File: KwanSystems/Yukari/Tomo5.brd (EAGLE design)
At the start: 43 parts, among them J101 USB_MICROB_JST, U101 FT232RLSSOP, U401 ATMEGA328P, U501 FGPMMOPA6H, U601 MPU9250, X501 uFL, Y401 16MHz

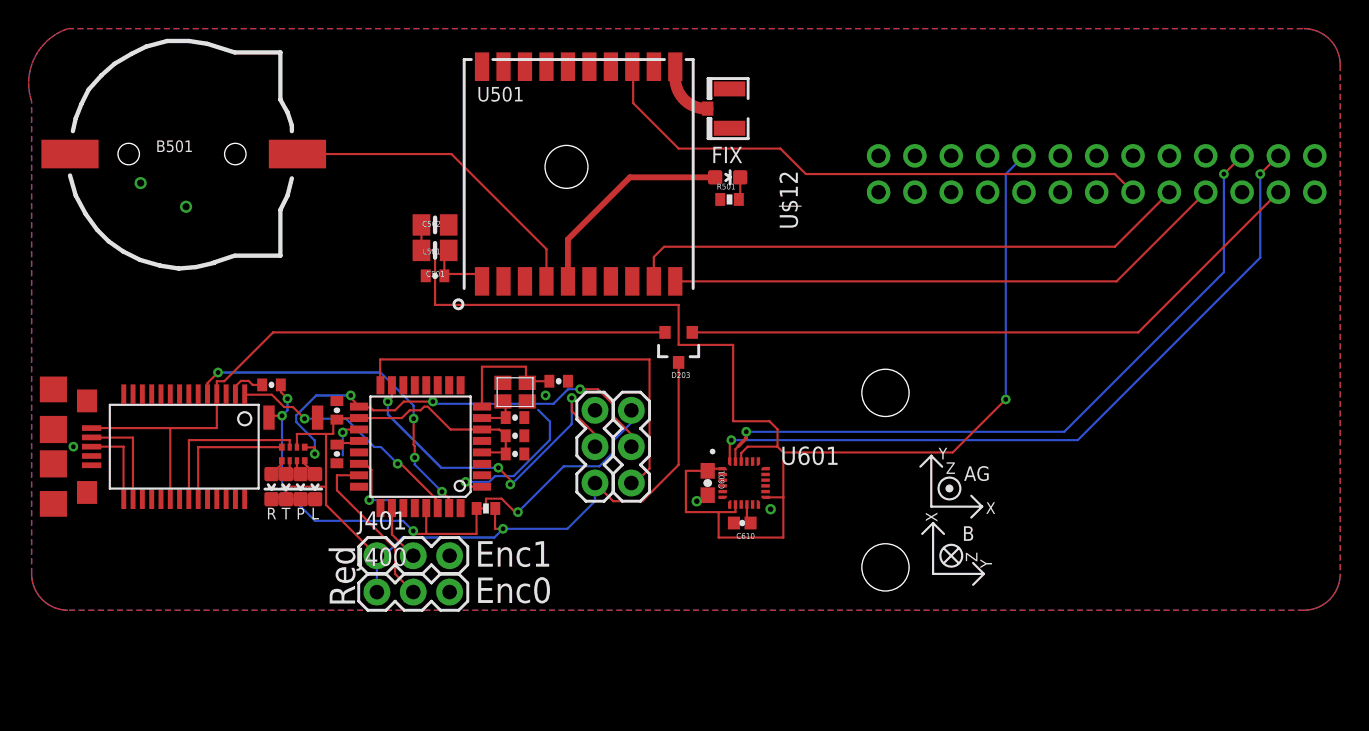
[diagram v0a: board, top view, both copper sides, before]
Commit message: Added Adafruit stuff
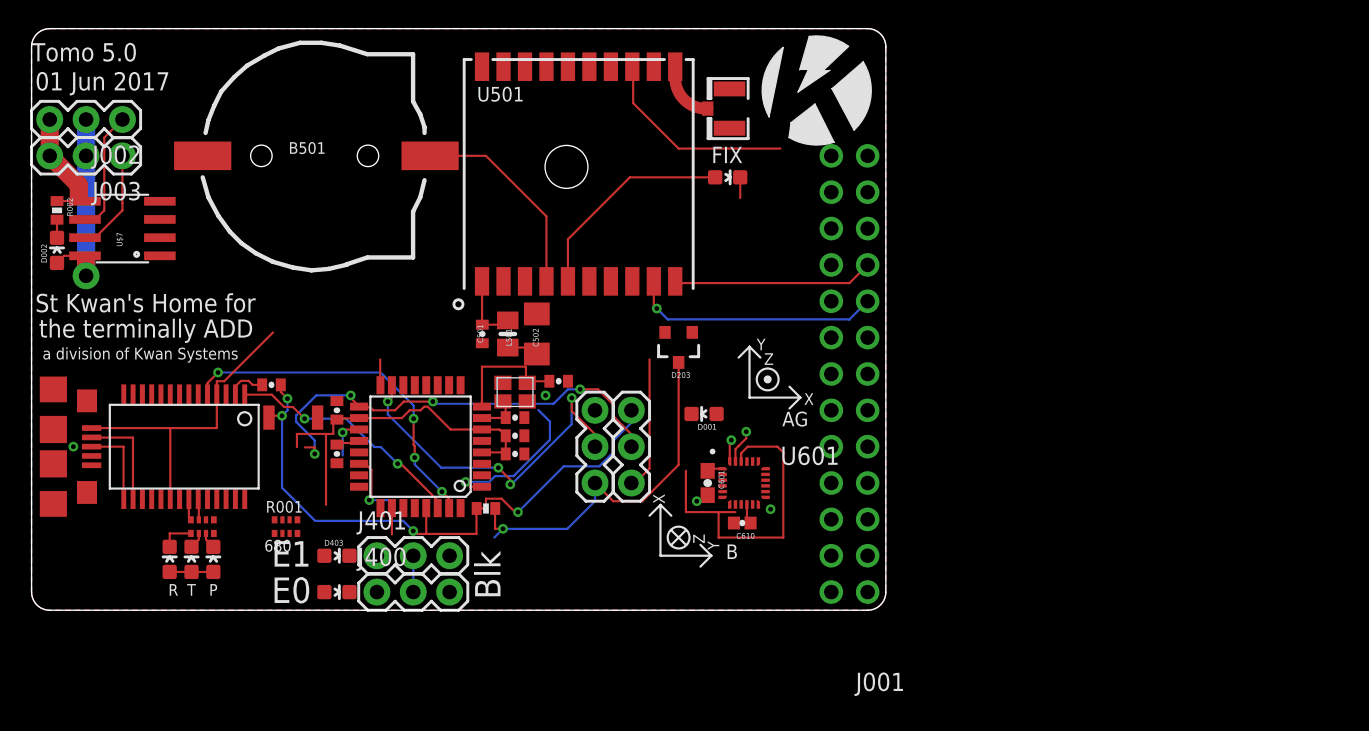
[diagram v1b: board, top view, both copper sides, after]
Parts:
- removed LOGO1: SFE_LOGO_FLAME.1_INCH, SparkFun-Aesthetics:SFE_LOGO_FLAME_.1
- removed LOGO2: OSHW-LOGOS, SparkFun-Aesthetics:OSHW-LOGO-S
- removed R501: 680, SparkFun-Passives:0402-RES
- removed STANDOFF1, STANDOFF2: STAND-OFF, SparkFun-Electromechanical:STAND-OFF
- removed U$12: PI_CONN, KwanSystems:PI_CONN
- added D001: RED, SparkFun-LED:LED-0603
- added D002: GREEN, SparkFun-LED:LED-0603
- added D403: YELLOW, SparkFun-LED:LED-0603
- added J001: PI_CONN, KwanSystems:PI_CONN
- added J002, J003: (no value), SparkFun-Connectors:1X03
- added R001: 680, KwanSystems:CRA04
- added R002: 10k, SparkFun-Passives:0402-RES
- added U$7: ADUM3221, KwanSystems:SO8N
- C502: device microbuilder:0805-NO -> SparkFun-Capacitors:1206
- moved U$1 55.7 mm to (54.9, 36.3), flipped to the top, turned to 0 degrees
- moved U$4 19.1 mm to (43.9, 3.81)
- moved U$3 14.8 mm to (50.2, 14.9)
- moved C502 10.4 mm to (35.3, 19.3), turned to 90 degrees
- moved B501 9.27 mm to (19.6, 31.8)
- moved D123 8.74 mm to (9.65, 3.56), turned to 0 degrees
- moved D122 8.33 mm to (11.2, 3.56), turned to 0 degrees
- moved R101 8.13 mm to (11.9, 5.84)
- moved D401 7.94 mm to (12.7, 3.56), turned to 0 degrees
- moved L501 7.74 mm to (33.3, 19.3), turned to 270 degrees
- moved D402 7.52 mm to (21.3, 1.27), turned to 270 degrees
- moved C501 5.24 mm to (31.5, 19.3), turned to 90 degrees
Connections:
- net D0 renamed D0/AT_RX
- net D1 renamed D1/AT_TX
- net D13 renamed D13/ENC0_ECHO+
- net N$8 renamed ENC0_ECHO-
- removed net 3V3: C502.1, C601.1, L501.2, U$12.3V3_1, U$12.3V3_2, U601.1, U601.13, U601.22, U601.8
- removed net D2: U401.32
- removed net D5: U401.9
- removed net D6: U401.10
- removed net ENC0: J400.2, U401.23
- removed net ENC1: J401.2, U401.26
- removed net N$11: D122.A, R101.2
- removed net N$9: D123.A, R101.1
- removed net RXLED1: R101.7, U101.22
- removed net SCL: U$12.SCL, U401.28, U601.23
- removed net SDA: U$12.SDA, U401.27, U601.24
- removed net TXLED1: R101.8, U101.23
- new net 3.3V: C502.1, C601.1, J001.3V3_1, J001.3V3_2, L501.2, U601.1, U601.13, U601.22, U601.8
- new net A0/ENC0: J400.1, U401.23
- new net A3/ENC1: J401.1, U401.26
- new net A4/SDA: J001.SDA, U401.27, U601.24
- new net A5/SCL: J001.SCL, U401.28, U601.23
- new net D2/ENC1_ECHO+: R001.6, U401.32
- new net D5/STEER+: U$7.2, U401.9
- new net D6/THROTTLE+: U$7.3, U401.10
- new net GND-ISO: J002.3, J003.3, R002.1, U$7.5
- new net IPWR-: D002.C, R002.2
- new net N$8: D403.A, R001.3
- new net PPS_ECHO-: D001.C, R001.2
- new net RXLED+: D123.C, R101.1
- new net RXLED-: R101.8, U101.22
- new net STEER-: J003.1, U$7.7
- new net THROTTLE-: J002.1, U$7.6
- new net TXLED+: D122.C, R101.2
- new net TXLED-: R101.7, U101.23
- new net VCC-ISO: D002.A, J002.2, J003.2, U$7.8
- net 1PPS: now also J001.#18; no longer U$12.#18
- net 5V: now also D122.A, D123.A, D401.A, J400.2, J401.2, U$7.1; no longer D122.C, D123.C, J400.1, J401.1, R101.6
- net 5V_PI: now also J001.5V0_1, J001.5V0_2; no longer U$12.5V0_1, U$12.5V0_2
- net GND: now also D403.C, J001.GND_1, J001.GND_2, J001.GND_3, J001.GND_4, J001.GND_5, R001.7, R001.8, R101.6, U$7.4; no longer D401.C, R501.1, U$12.GND_1, U$12.GND_2, U$12.GND_3, U$12.GND_4, U$12.GND_5
- net GO_BTN: now also J001.#17; no longer U$12.#17
- net GPS_RX: now also J001.TXD; no longer U$12.TXD
- net GPS_TX: now also J001.RXD; no longer U$12.RXD
- net N$5: now also D401.C; no longer D401.A
- net N$6: now also R001.1; no longer R501.2
- net PPS_ECHO+: now also D001.A, J001.#22; no longer U$12.#22
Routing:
- net 3V3: track 101.3 -> 0.00 mm, vias 1 -> 0
- net SDA: track 51.3 -> 0.00 mm, vias 2 -> 0
- net SCL: track 49.0 -> 0.00 mm, vias 2 -> 0
- net 5V_PI: track 45.0 -> 0.00 mm
- net VBUS: track 49.7 -> 22.3 mm
- net 1PPS: track 40.1 -> 14.2 mm
- net 3.3V: track 0.00 -> 25.7 mm
- net GPS_RX: track 39.6 -> 14.0 mm
- net GPS_TX: track 39.6 -> 17.6 mm, vias 0 -> 1
- net D12: track 30.0 -> 11.1 mm
- net 5V: track 73.5 -> 57.7 mm
- net VCC-ISO: track 0.00 -> 14.5 mm, vias 0 -> 1
- net ENC0: track 11.9 -> 0.00 mm
- net RXLED1: track 11.7 -> 0.00 mm
- net TXLED1: track 9.47 -> 0.00 mm
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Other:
- board outline added: 59.7 x 40.6 mm
- board text added: "01 Jun 2017"
- board text added: "Blk"
- board text added: "E0"
- board text added: "E1"
- board text added: "Tomo 5.0"
- board text removed: "20 Nov 2012"
- board text removed: "3V"
- board text removed: "BAT"
- board text removed: "Backup Battery: CR1220"
- board text removed: "EN"
- board text removed: "Enc0"
- board text removed: "Enc1"
- board text removed: "GND"
- board text removed: "L"
- board text removed: "Naninator 1.0"
- board text removed: "Opt. Active Ant."
- board text removed: "RST"
- board text removed: "Red"
- board text removed: "TX"
- board text removed: "USB"
- board text removed: "Ultimate GPS FeatherWing"
